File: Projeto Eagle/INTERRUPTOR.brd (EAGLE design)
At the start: 39.8 x 21.5 mm, 6 parts, among them J1 CONECTOR, J2 CONECTOR, U1 74HC132

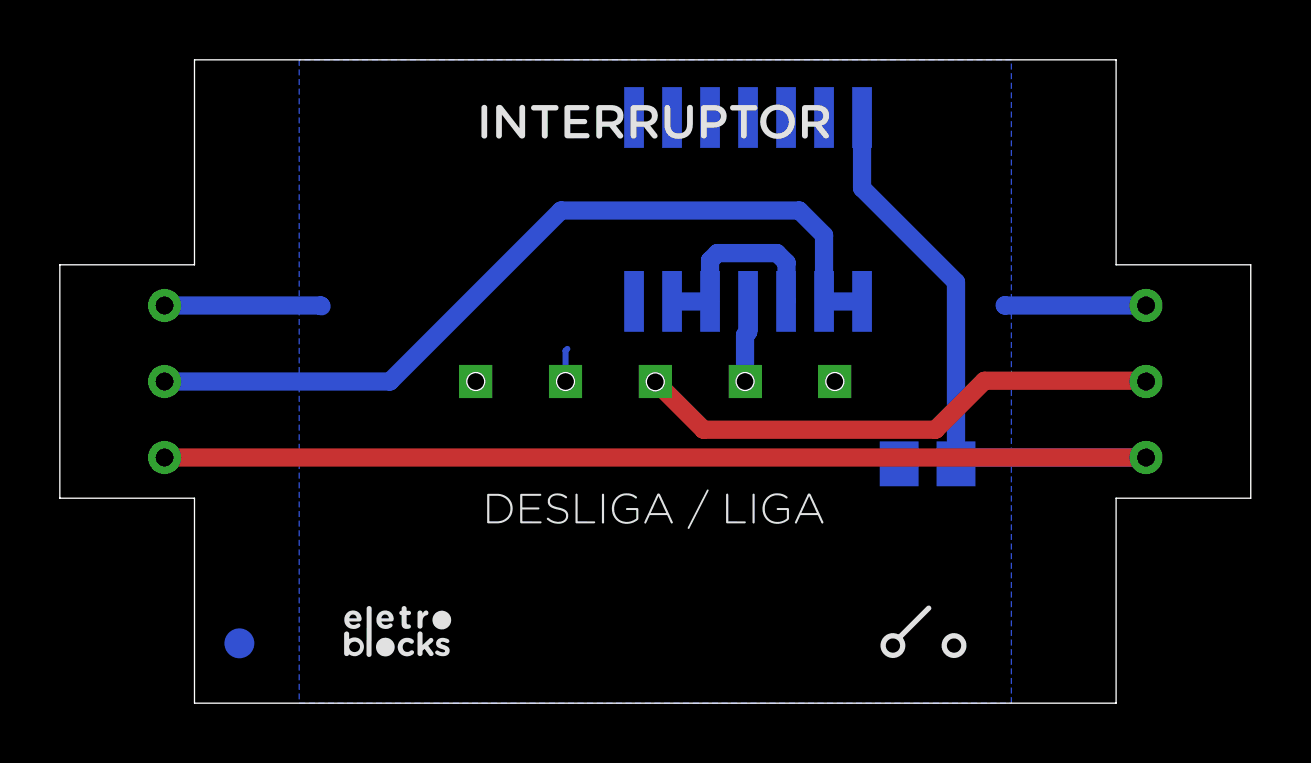
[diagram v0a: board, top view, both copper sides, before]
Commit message: correção de pads, adição de label para versionamento e plano de VCC
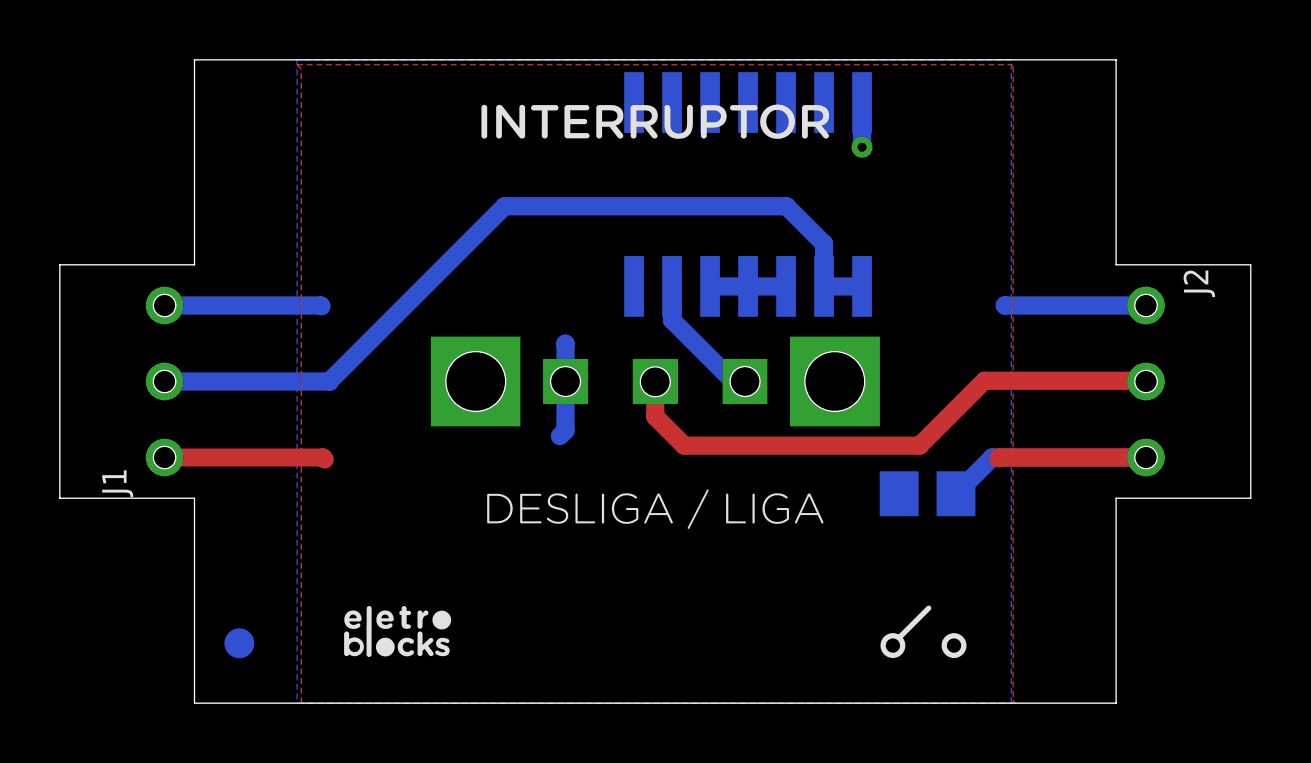
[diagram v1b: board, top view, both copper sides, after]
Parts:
- J1: value CONECTOR -> CONECTOR_MACHO
- J2: value CONECTOR -> CONECTOR_FEMEA
- U1: device 40xx:SO14 -> 74xx-eu:SO14
- moved C1 1.00 mm to (21.0, 7.00)
- moved U1 0.50 mm to (15.0, 17.0)
- renumbered U$1 to J3
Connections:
- net N$2: now also U1.4; no longer U1.6
- net N$3: now also U1.6; no longer U1.4
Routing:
- net VCC: track 52.1 -> 18.7 mm, vias 0 -> 1
- net N$2: track 6.73 -> 2.54 mm
- net GND: track 11.1 -> 13.2 mm
- net N$3: track 2.72 -> 4.41 mm
- net SIGNAL_OUT: track 17.8 -> 18.9 mm
- net SIGNAL_IN: track 28.2 -> 27.7 mm
- added copper zone on layer 1, net VCC
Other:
- board text added: "V1.0.1"
